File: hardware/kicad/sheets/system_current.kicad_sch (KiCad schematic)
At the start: 5 parts, among them U20 INA237AIDGSR

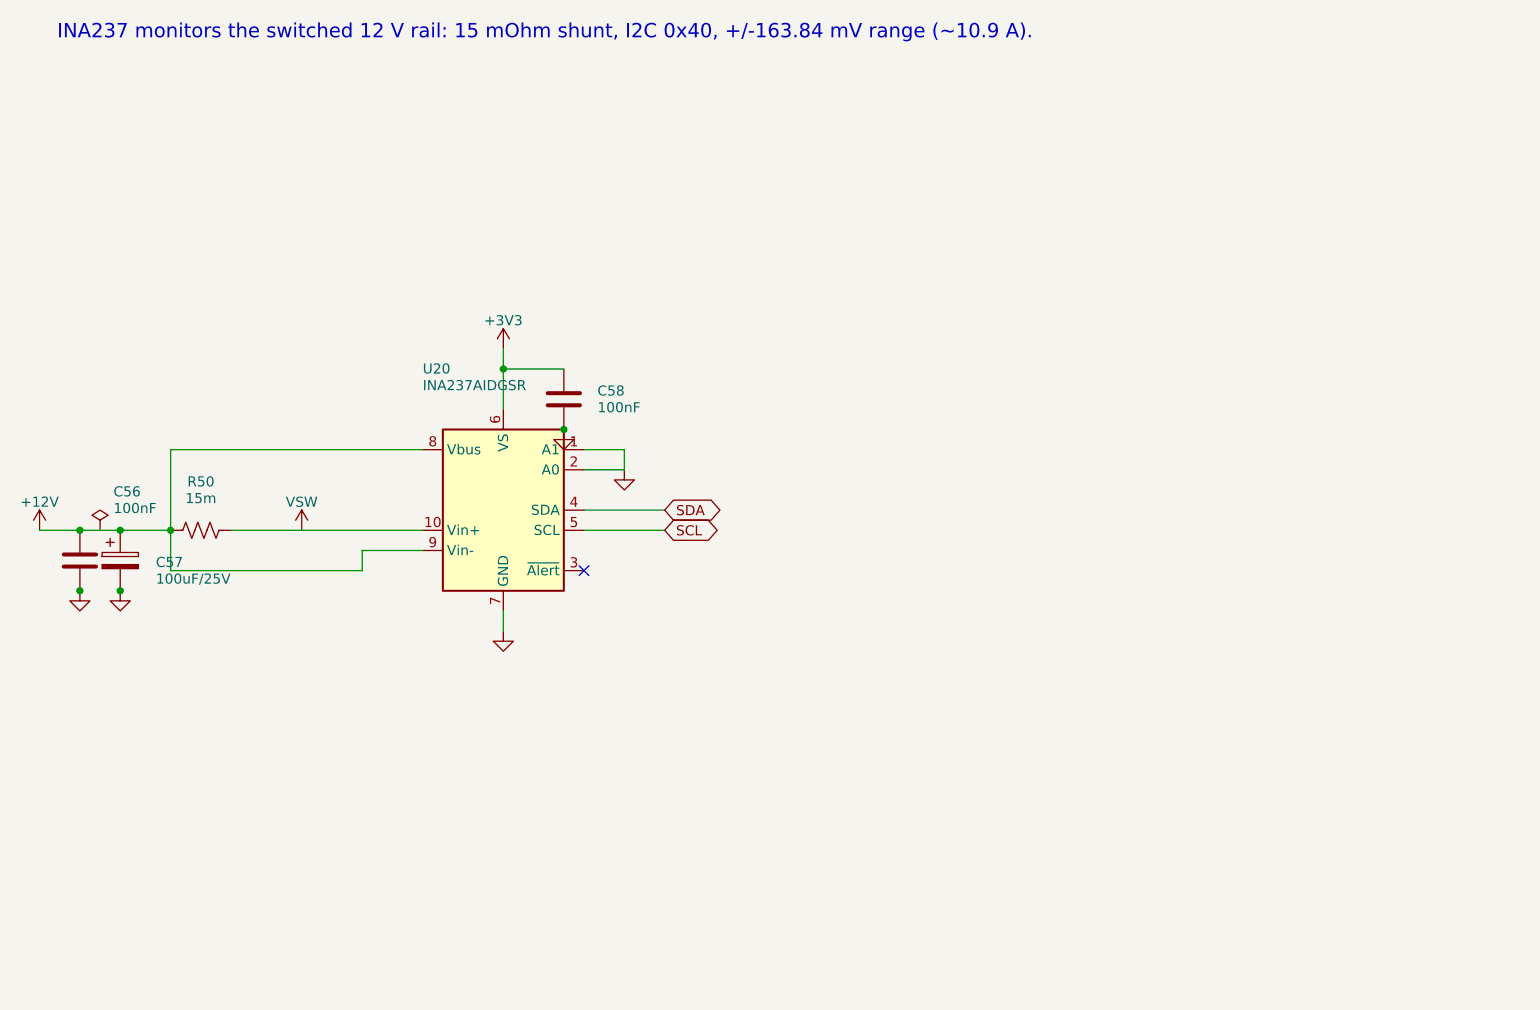
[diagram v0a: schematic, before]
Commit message: KiCad: cleaner layout, decoupling blocks, label directions, KiCad format fixes
- move IC decoupling caps into labelled blocks at the side of each sheet
- global labels show input/output direction per net
- no 4-way junctions (generator now checks and fails)
- generator output matches KiCad's saved format (hide property, junction
  and wire normalisation, lib symbol embedded fonts, multi-unit pins)
- hand-laid USB ESD protection as a pass-through

Co-Authored-By: Claude Sonnet 5.5 <noreply@anthropic.com>
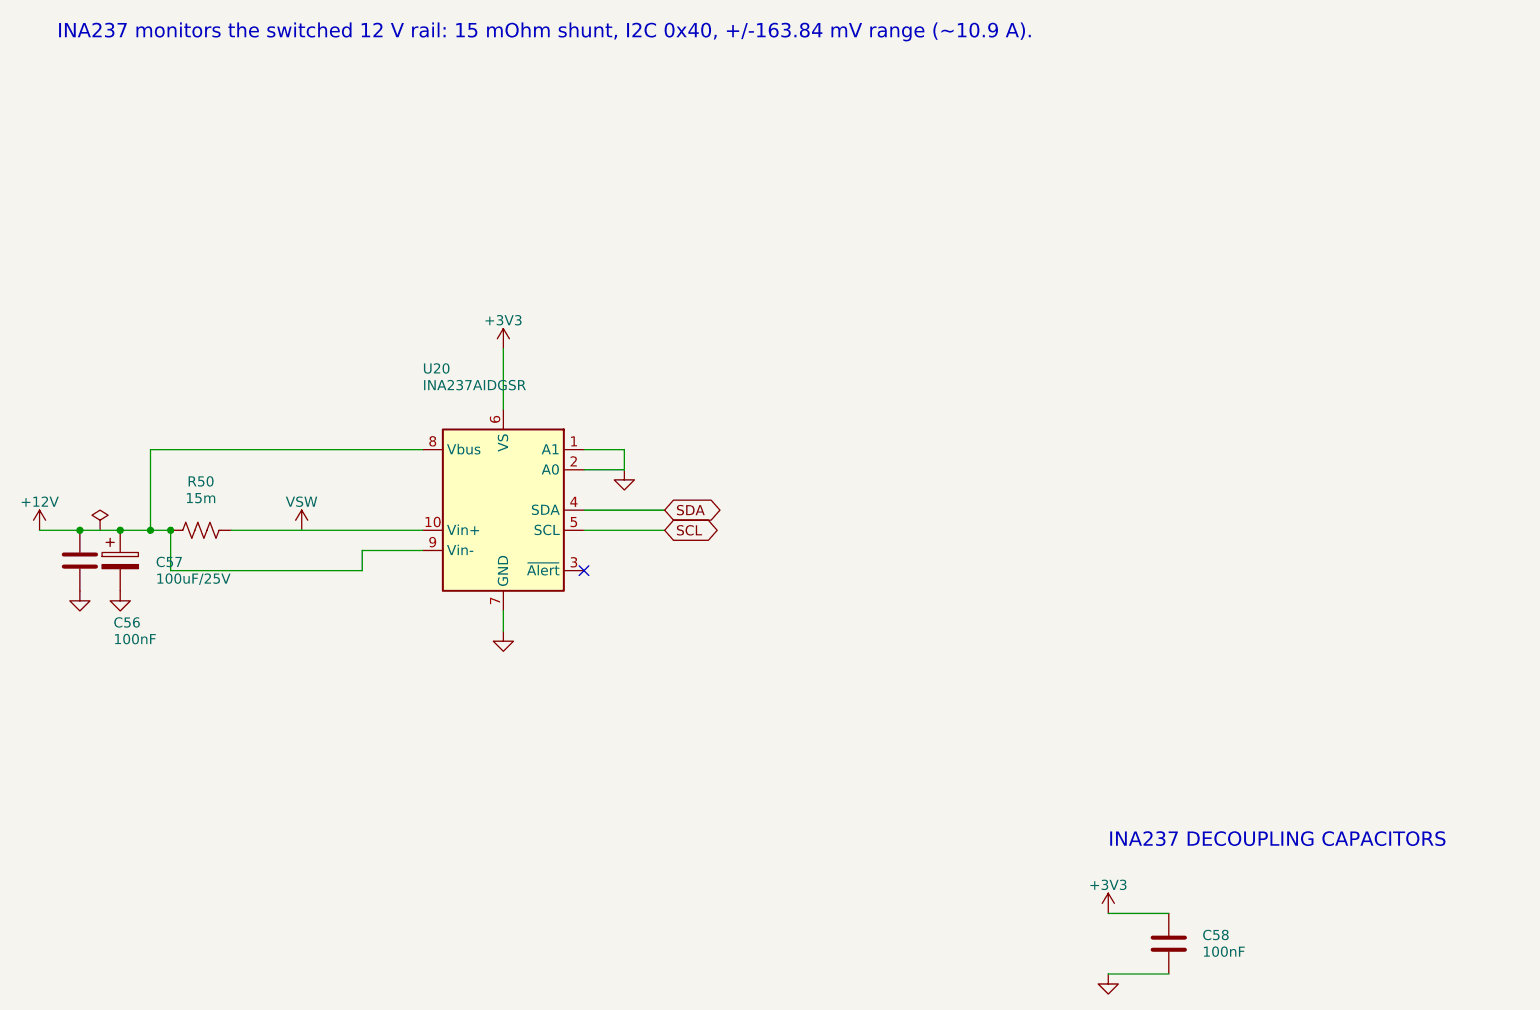
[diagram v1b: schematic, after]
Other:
- note added: "INA237 DECOUPLING CAPACITORS"
